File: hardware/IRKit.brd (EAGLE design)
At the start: 54 x 56 mm, 69 parts, among them CN1 USB-CONNECTORMICROB, IC1 ATMEGA32U4AU, IC2 TLV70233DBVT, IC3 LM386MM-1, IC4 GS1011MXXS, SW1 EVQPUJ02K, T1 2SD1781K, T2 BSS138

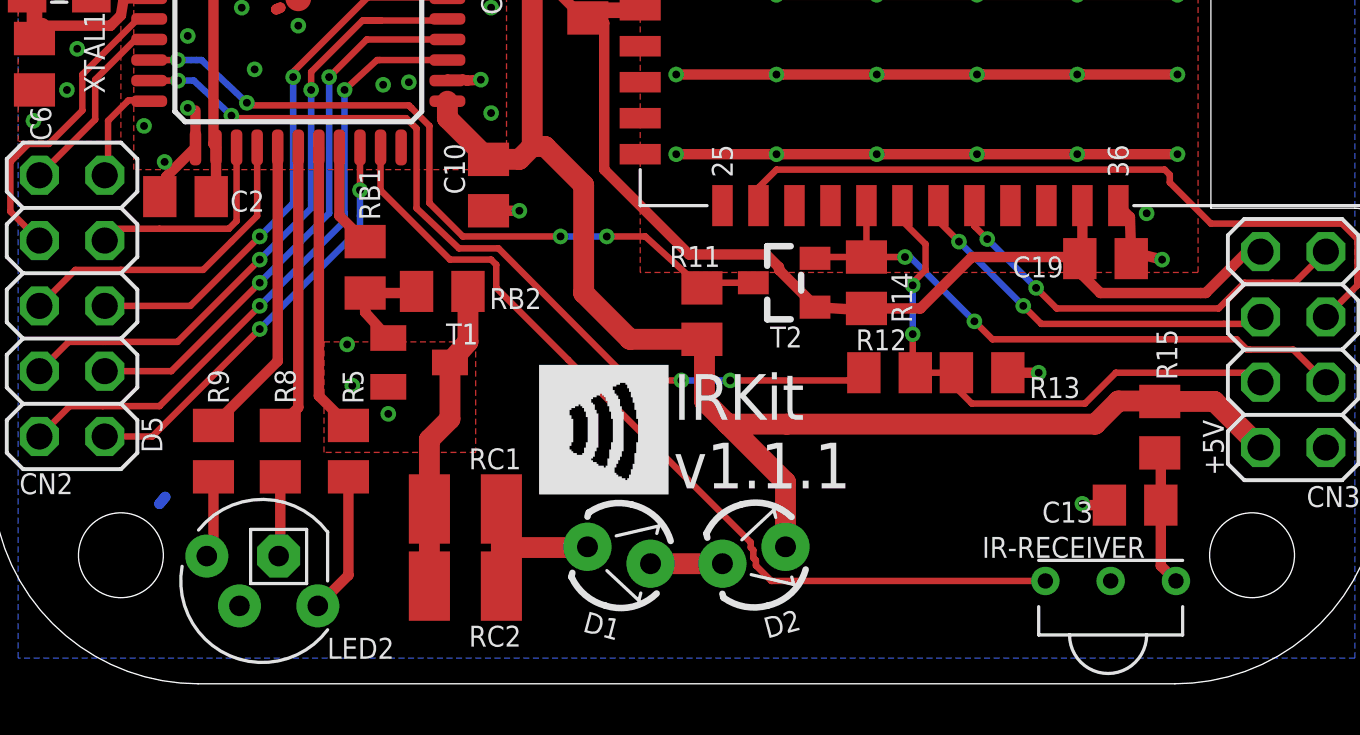
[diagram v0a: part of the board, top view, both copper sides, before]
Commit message: moved full color led and ir receiver inside 1mm, to avoid collision with screw bosses
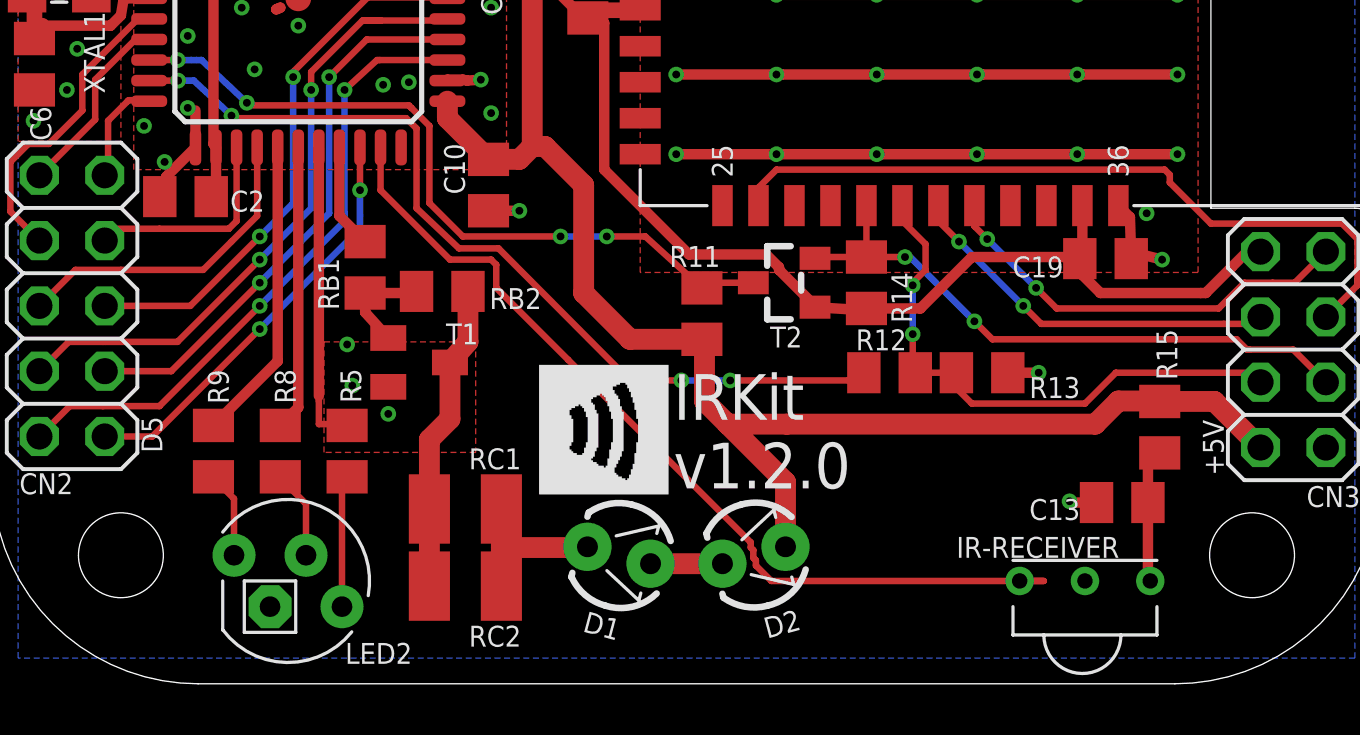
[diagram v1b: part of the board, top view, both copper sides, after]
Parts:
- moved IR-RECEIVER 1.00 mm to (42.5, 4.00)
- moved LED2 1.00 mm to (11.5, 4.00), turned to 0 degrees
- moved C13 0.51 mm to (44.0, 7.05)
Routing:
- net D13/IRIN: track 34.8 -> 35.6 mm
- net GND: track 180.3 -> 179.7 mm
- net D9/LED_G: track 11.3 -> 11.9 mm
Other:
- board text added: "IRKit v1.2.0"
- board text removed: "IRKit v1.1.1"
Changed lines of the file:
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@@
 <text x="47.9" y="8.1" size="0.8128" layer="21" rot="R90">+5V</text>
 <text x="26.5" y="7.6" size="1.778" layer="21">IRKit
-v1.1.1</text>
+v1.2.0</text>
 <dimension x1="54" y1="8" x2="0" y2="8" x3="27" y3="-3.1" textsize="1.778" layer="51"/>
 <dimension x1="5" y1="5" x2="8.8" y2="0" x3="-1.1" y3="2.5" textsize="1.778" layer="51" dtype="vertical"/>
@@
 <attribute name="VALUE" x="-0.945" y="45.31" size="0.8128" layer="27" rot="R270"/>
 </element>
-<element name="IR-RECEIVER" library="my" package="IR-RECEIVER" value="PL-IRM2161" x="43.5" y="4" smashed="yes">
-<attribute name="NAME" x="38.5" y="4.9" size="0.8128" layer="25"/>
+<element name="IR-RECEIVER" library="my" package="IR-RECEIVER" value="PL-IRM2161" x="42.5" y="4" smashed="yes">
+<attribute name="NAME" x="37.5" y="4.9" size="0.8128" layer="25"/>
 </element>
 <element name="R15" library="my" package="SMD2012" value="220" x="45.4085" y="9.982" smashed="yes" rot="R90">
@@
 <attribute name="VALUE" x="8.914" y="9.812" size="0.8128" layer="27" rot="R270"/>
 </element>
-<element name="R5" library="my" package="SMD2012" value="2.2k" x="13.85" y="9.05" smashed="yes" rot="R270">
-<attribute name="NAME" x="14.434" y="10.888" size="0.8128" layer="25" rot="R90"/>
-<attribute name="VALUE" x="11.564" y="9.812" size="0.8128" layer="27" rot="R270"/>
-</element>
 <element name="R1" library="my" package="SMD2012" value="10k" x="2.5" y="36.525" smashed="yes">
 <attribute name="NAME" x="4.338" y="35.741" size="0.8128" layer="25"/>
@@
 <attribute name="VALUE" x="3.9235" y="23.338" size="0.8128" layer="27" rot="R90"/>
 </element>
-<element name="C13" library="my" package="SMD2012" value="4.7uF" x="44.45" y="6.95" smashed="yes" rot="R180">
-<attribute name="NAME" x="42.812" y="7.084" size="0.8128" layer="25" rot="R180"/>
-<attribute name="VALUE" x="45.212" y="9.236" size="0.8128" layer="27" rot="R180"/>
-</element>
-<element name="LED2" library="my" package="LED5MMRGB" value="5MMRGBLED" x="10.5" y="4" smashed="yes" rot="R180">
-<attribute name="NAME" x="13.025" y="0.975" size="0.8128" layer="21"/>
+<element name="C13" library="my" package="SMD2012" value="4.7uF" x="43.95" y="7.05" smashed="yes" rot="R180">
+<attribute name="NAME" x="42.312" y="7.184" size="0.8128" layer="25" rot="R180"/>
+<attribute name="VALUE" x="44.712" y="9.336" size="0.8128" layer="27" rot="R180"/>
 </element>
 <element name="IC4" library="my" package="GS1011MXXS" value="GS1011MXXS" x="25.2" y="38" smashed="yes" rot="R270">
@@
 </element>
 <element name="RB1" library="my" package="SMD2012" value="1.8k" x="14.5" y="16.2" smashed="yes" rot="R90">
-<attribute name="NAME" x="15.084" y="18.038" size="0.8128" layer="25" rot="R90"/>
+<attribute name="NAME" x="13.484" y="14.538" size="0.8128" layer="25" rot="R90"/>
 <attribute name="VALUE" x="16.786" y="15.438" size="0.8128" layer="27" rot="R90"/>
 </element>
@@
 <attribute name="NAME" x="25.975" y="44.4" size="0.8128" layer="25" rot="R270"/>
 <attribute name="VALUE" x="23.1" y="44.2" size="1.016" layer="27" rot="R270"/>
+</element>
+<element name="LED2" library="my" package="LED5MMRGB" value="5MMRGBLED" x="11.5" y="4" smashed="yes">
+<attribute name="NAME" x="13.725" y="0.775" size="0.8128" layer="21"/>
+</element>
+<element name="R5" library="my" package="SMD2012" value="2.2k" x="13.8" y="9.05" smashed="yes" rot="R270">
+<attribute name="NAME" x="14.35" y="10.925" size="0.8128" layer="25" rot="R90"/>
+<attribute name="VALUE" x="11.9" y="10.05" size="1.016" layer="27" rot="R270"/>
 </element>
 </elements>
@@
 <contactref element="IC4" pad="36"/>
 <contactref element="C18" pad="1"/>
-<contactref element="LED2" pad="3"/>
 <contactref element="C12" pad="-"/>
 <contactref element="C10" pad="1"/>
@@
 <via x="11.9" y="27.7" extent="1-16" drill="0.3048"/>
 <wire x1="11.9" y1="26.6625" x2="11.9" y2="27.7" width="0.4064" layer="1"/>
-<wire x1="6.5" y1="7" x2="6.724025" y2="7.2669875" width="0.4064" layer="16"/>
-<wire x1="6.5" y1="7" x2="6.724025" y2="7.2669875" width="0.4064" layer="16"/>
 <via x="20.5" y="18.4" extent="1-16" drill="0.3048"/>
 <via x="32.8" y="51.7" extent="1-16" drill="0.3048"/>
@@
 <wire x1="31.6" y1="51.9" x2="31.8" y2="51.7" width="0.6096" layer="1"/>
 <wire x1="31.8" y1="51.7" x2="32.8" y2="51.7" width="0.6096" layer="1"/>
-<via x="42.4" y="7" extent="1-16" drill="0.3048"/>
-<wire x1="43.45" y1="6.95" x2="42.45" y2="6.95" width="0.4064" layer="1"/>
-<wire x1="42.45" y1="6.95" x2="42.4" y2="7" width="0.4064" layer="1"/>
-<polygon width="1.016" layer="1">
+<via x="41.9" y="7.1" extent="1-16" drill="0.3048"/>
+<wire x1="42.95" y1="7.05" x2="41.95" y2="7.05" width="0.4064" layer="1"/>
+<wire x1="41.95" y1="7.05" x2="41.9" y2="7.1" width="0.4064" layer="1"/>
+<polygon width="0.8128" layer="1">
 <vertex x="12.9" y="13.3"/>
 <vertex x="18.8" y="13.3"/>
@@
 <wire x1="34.3" y1="40.2" x2="34.4" y2="40.1" width="0.4064" layer="1"/>
 <wire x1="19.6" y1="31.8" x2="19.6" y2="31" width="0.8128" layer="1"/>
+<contactref element="LED2" pad="3"/>
 </signal>
 <signal name="N$10">
@@
 <contactref element="R15" pad="1"/>
 <contactref element="C13" pad="1"/>
-<wire x1="45.45" y1="6.95" x2="45.45" y2="4.59" width="0.4064" layer="1"/>
-<wire x1="45.45" y1="4.59" x2="46.04" y2="4" width="0.4064" layer="1"/>
-<wire x1="45.45" y1="6.95" x2="45.45" y2="8.9405" width="0.4064" layer="1"/>
-<wire x1="45.45" y1="8.9405" x2="45.4085" y2="8.982" width="0.4064" layer="1"/>
-</signal>
-<signal name="N$15">
-<contactref element="R8" pad="2"/>
-<contactref element="LED2" pad="2"/>
-<wire x1="11.2" y1="8.05" x2="11.2" y2="5.0334" width="0.4064" layer="1"/>
-<wire x1="11.2" y1="5.0334" x2="11.135" y2="4.9684" width="0.4064" layer="1"/>
-</signal>
-<signal name="N$17">
-<contactref element="R5" pad="2"/>
-<contactref element="LED2" pad="1"/>
-<wire x1="13.85" y1="8.05" x2="13.85" y2="4.2226" width="0.4064" layer="1"/>
-<wire x1="13.85" y1="4.2226" x2="12.659" y2="3.0316" width="0.4064" layer="1"/>
-</signal>
-<signal name="N$5">
-<contactref element="LED2" pad="4"/>
-<contactref element="R9" pad="2"/>
-<wire x1="8.6" y1="8.05" x2="8.6" y2="5.2274" width="0.4064" layer="1"/>
-<wire x1="8.6" y1="5.2274" x2="8.341" y2="4.9684" width="0.4064" layer="1"/>
+<wire x1="45.4085" y1="8.982" x2="44.95" y2="8.5235" width="0.4064" layer="1"/>
+<wire x1="44.95" y1="8.5235" x2="44.95" y2="7.05" width="0.4064" layer="1"/>
+<wire x1="44.95" y1="7.05" x2="44.95" y2="4.09" width="0.4064" layer="1"/>
+<wire x1="44.95" y1="4.09" x2="45.04" y2="4" width="0.4064" layer="1"/>
 </signal>
 <signal name="D10/IROUT">
@@
 <wire x1="30.3" y1="4" x2="29.7" y2="4.6" width="0.254" layer="1"/>
 <wire x1="40.9" y1="4" x2="30.3" y2="4" width="0.254" layer="1"/>
-<wire x1="40.9" y1="4" x2="40.96" y2="4" width="0.254" layer="1"/>
+<wire x1="40.9" y1="4" x2="39.96" y2="4" width="0.254" layer="1"/>
 <wire x1="15.1" y1="20.8625" x2="15.1" y2="19.2" width="0.254" layer="1"/>
 <wire x1="15.1" y1="19.2" x2="17.8" y2="16.5" width="0.254" layer="1"/>
@@
 <signal name="D9/LED_G">
 <contactref element="IC1" pad="29"/>
+<wire x1="12.7" y1="20.8625" x2="12.7" y2="11.2" width="0.4064" layer="1"/>
 <contactref element="R5" pad="1"/>
-<wire x1="12.7" y1="20.8625" x2="12.7" y2="11.2" width="0.4064" layer="1"/>
-<wire x1="12.7" y1="11.2" x2="13.85" y2="10.05" width="0.4064" layer="1"/>
+<wire x1="12.7" y1="10.1" x2="13.8" y2="10.1" width="0.254" layer="1"/>
+<wire x1="12.7" y1="11" x2="12.7" y2="10.1" width="0.254" layer="1"/>
+<wire x1="13.8" y1="10.1" x2="13.8" y2="10.05" width="0.254" layer="1"/>
+<wire x1="12.7" y1="11" x2="12.7" y2="11.2" width="0.254" layer="1"/>
 </signal>
 <signal name="D8/LED_B">
@@
 <wire x1="25" y1="45.9" x2="25" y2="44.2" width="0.254" layer="1"/>
 </signal>
+<signal name="N$17">
+<contactref element="R8" pad="2"/>
+<contactref element="LED2" pad="2"/>
+<wire x1="12.2" y1="7" x2="11.2" y2="8" width="0.254" layer="1"/>
+<wire x1="12.2" y1="5" x2="12.2" y2="7" width="0.254" layer="1"/>
+<wire x1="11.2" y1="8" x2="11.2" y2="8.05" width="0.254" layer="1"/>
+</signal>
+<signal name="N$41">
+<contactref element="LED2" pad="4"/>
+<contactref element="R9" pad="2"/>
+<wire x1="9.4" y1="7.2" x2="8.6" y2="8" width="0.254" layer="1"/>
+<wire x1="9.4" y1="5" x2="9.4" y2="7.2" width="0.254" layer="1"/>
+<wire x1="8.6" y1="8" x2="8.6" y2="8.05" width="0.254" layer="1"/>
+</signal>
+<signal name="N$5">
+<contactref element="LED2" pad="1"/>
+<contactref element="R5" pad="2"/>
+<wire x1="13.6" y1="7.8" x2="13.8" y2="8" width="0.254" layer="1"/>
+<wire x1="13.6" y1="3" x2="13.6" y2="7.8" width="0.254" layer="1"/>
+<wire x1="13.8" y1="8" x2="13.8" y2="8.05" width="0.254" layer="1"/>
+</signal>
 </signals>
